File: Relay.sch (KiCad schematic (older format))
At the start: 12 parts

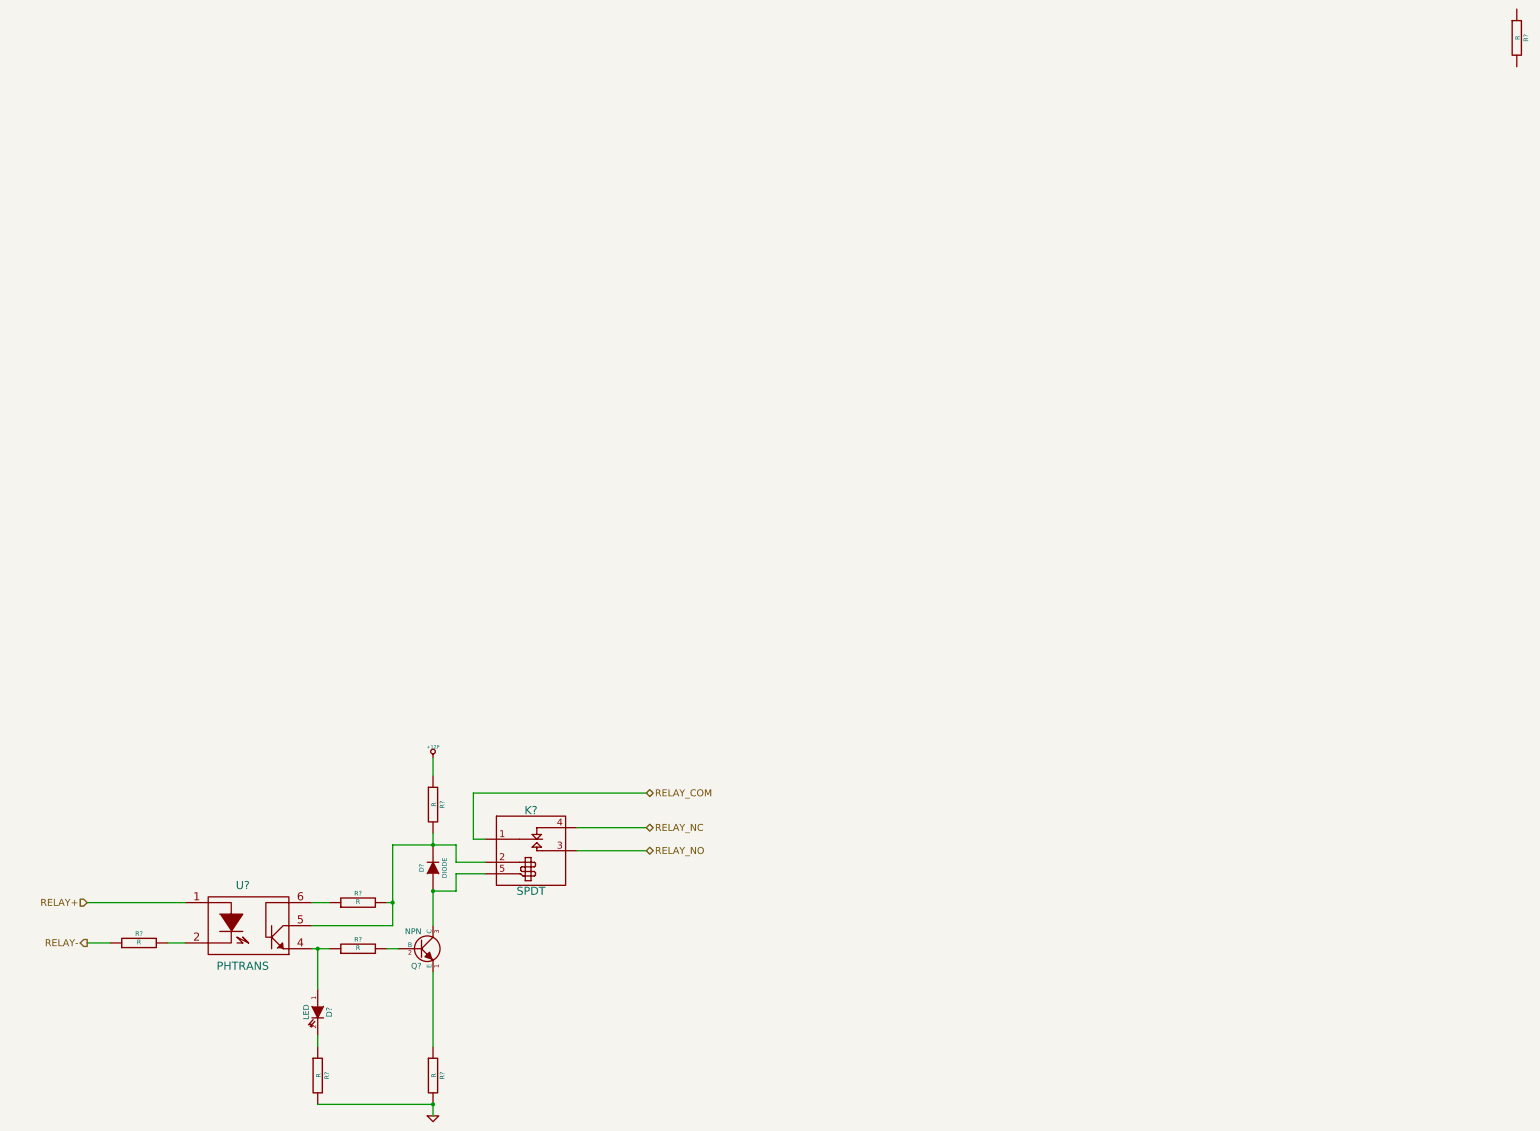
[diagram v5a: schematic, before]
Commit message: Preliminary Module Layouts
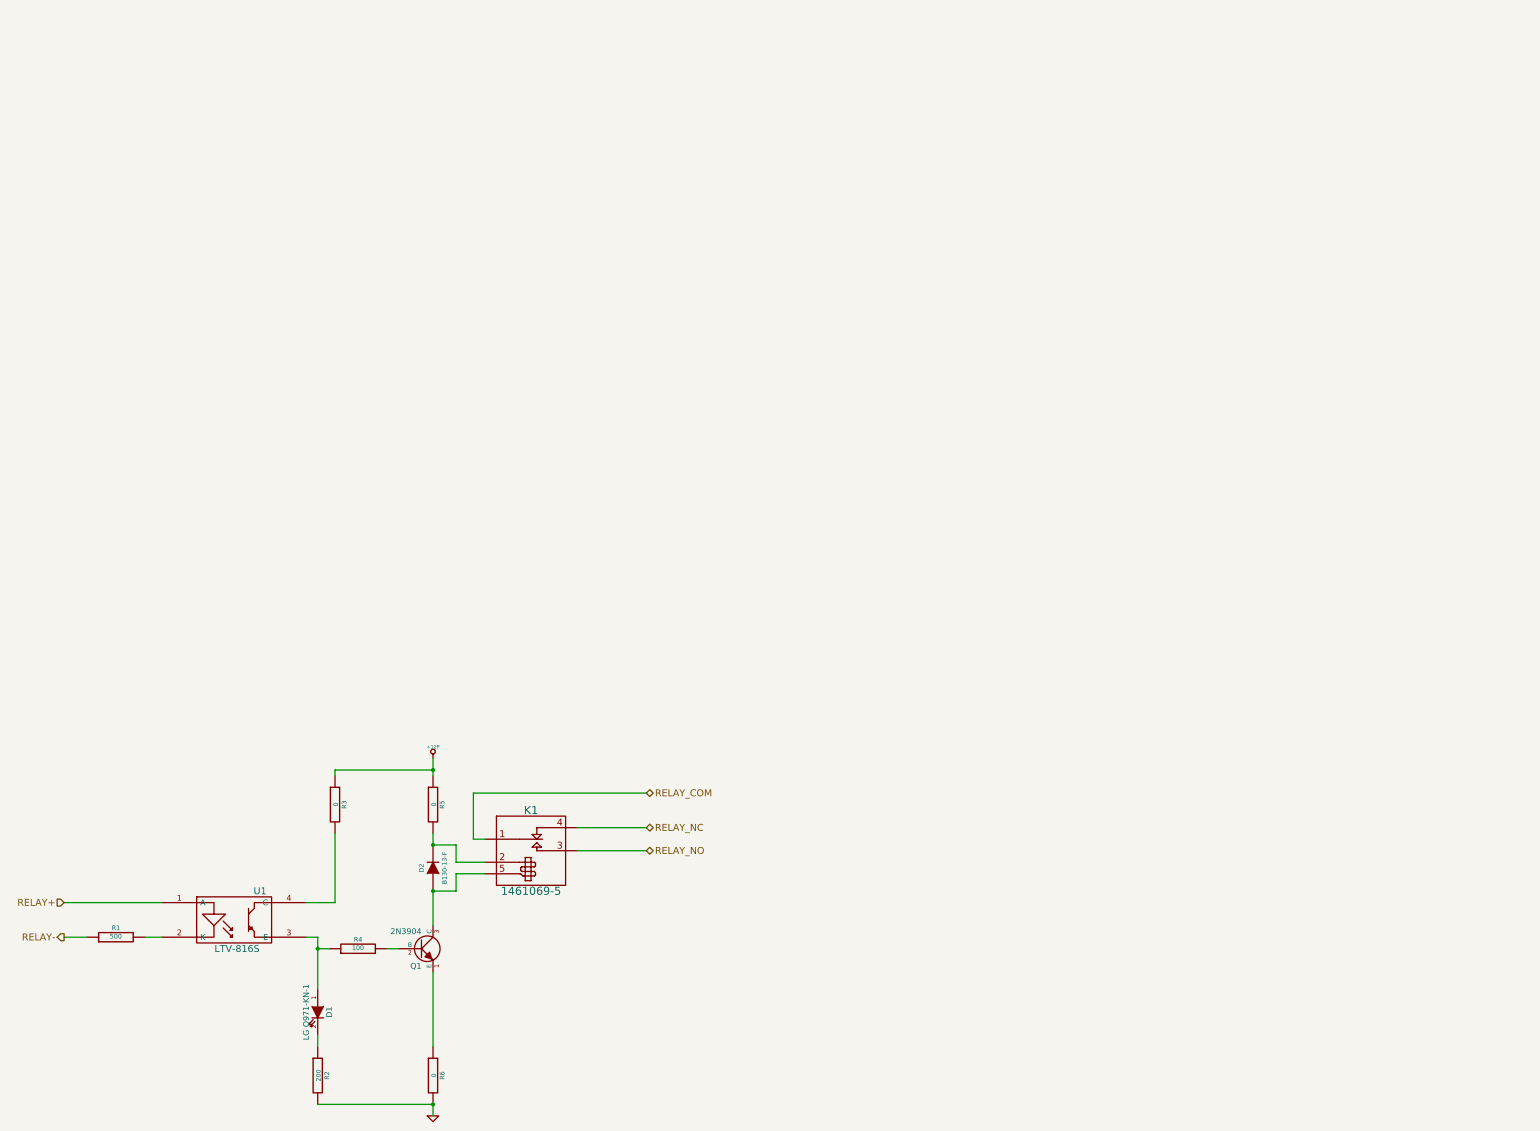
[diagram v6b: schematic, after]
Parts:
- removed R? (x2): R, ~, symbol R
- removed U?: PHTRANS, ~, symbol PHTRANS
- added R3: 0, ~, symbol R
- added U1: LTV-816S, symbol OPTO-TRANSISTOR4
- D1: renamed from D?; value LED -> LG Q971-KN-1
- D2: renamed from D?; value DIODE -> B130-13-F
- K1: renamed from K?; value SPDT -> 1461069-5; MFG Part Number (none) -> 1461069-5
- Q1: renamed from Q?; value NPN -> 2N3904; MFG Name (none) -> Diodes Inc; MFG Part Number (none) -> MMBT3904-7-F
- R1: renamed from R?; value R -> 500
- R2: renamed from R?; value R -> 200
- R4: renamed from R?; value R -> 100
- R5, R6: renamed from R?; value R -> 0
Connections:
- net +12P: now also R3.1
- net RELAY+: now also U1.1 (A)
- net at R1.2: now also U1.2 (K)
- net at D1.1 (A), R4.1: now also U1.3 (E)
- new net: R3.2, U1.4 (C)
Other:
- moved on the sheet: R1
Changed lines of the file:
@@
 $Descr A4 11693 8268
 encoding utf-8
-Sheet 7 9
+Sheet 6 9
 Title ""
-Date "30 sep 2013"
+Date "15 oct 2013"
 Rev ""
 Comp ""
@@
 Comment4 ""
 $EndDescr
-Text HLabel 4750 3350 0    60   Input ~ 0
+Text HLabel 4550 3350 0    60   Input ~ 0
 RELAY+
-Text HLabel 4750 3700 0    60   Output ~ 0
+Text HLabel 4550 3650 0    60   Output ~ 0
 RELAY-
 Text HLabel 9600 2700 2    60   BiDi ~ 0
@@
 Text HLabel 9600 2900 2    60   BiDi ~ 0
 RELAY_NO
-$Comp
-L R R?
-U 1 1 523D0C55
-P 17150 -4150
-F 0 "R?" V 17230 -4150 40  0000 C CNN
-F 1 "R" V 17157 -4149 40  0000 C CNN
-F 2 "~" V 17080 -4150 30  0000 C CNN
-F 3 "~" H 17150 -4150 30  0000 C CNN
-	1    17150 -4150
-	1    0    0    -1
-$EndComp
 Text HLabel 9600 2400 2    60   BiDi ~ 0
 RELAY_COM
 $Comp
-L SPDT K?
+L SPDT K1
 U 1 1 523D17C5
 P 8600 2750
-F 0 "K?" H 8600 2950 70  0000 C CNN
-F 1 "SPDT" H 8600 2250 70  0000 C CNN
+F 0 "K1" H 8600 2950 70  0000 C CNN
+F 1 "1461069-5	" H 8600 2250 70  0000 C CNN
 F 2 "~" H 8600 2750 60  0000 C CNN
 F 3 "~" H 8600 2750 60  0000 C CNN
+F 4 "1461069-5" H 8600 2750 60  0001 C CNN "MFG Part Number"
 	1    8600 2750
 	1    0    0    -1
 $EndComp
 $Comp
-L NPN Q?
+L NPN Q1
 U 1 1 523D17DC
 P 7650 3750
-F 0 "Q?" H 7650 3600 50  0000 R CNN
-F 1 "NPN" H 7650 3900 50  0000 R CNN
+F 0 "Q1" H 7650 3600 50  0000 R CNN
+F 1 "2N3904" H 7650 3900 50  0000 R CNN
 F 2 "~" H 7650 3750 60  0000 C CNN
 F 3 "~" H 7650 3750 60  0000 C CNN
+F 4 "Diodes Inc" H 7650 3750 60  0001 C CNN "MFG Name"
+F 5 "MMBT3904-7-F" H 7650 3750 60  0001 C CNN "MFG Part Number"
 	1    7650 3750
 	1    0    0    -1
 $EndComp
 $Comp
-L DIODE D?
+L DIODE D2
 U 1 1 523D17F8
 P 7750 3050
-F 0 "D?" H 7750 3150 40  0000 C CNN
-F 1 "DIODE" H 7750 2950 40  0000 C CNN
+F 0 "D2" H 7750 3150 40  0000 C CNN
+F 1 "B130-13-F" H 7750 2950 40  0000 C CNN
 F 2 "~" H 7750 3050 60  0000 C CNN
 F 3 "~" H 7750 3050 60  0000 C CNN
@@
 $EndComp
 $Comp
-L R R?
+L R R2
 U 1 1 523D1807
 P 6750 4850
-F 0 "R?" V 6830 4850 40  0000 C CNN
-F 1 "R" V 6757 4851 40  0000 C CNN
+F 0 "R2" V 6830 4850 40  0000 C CNN
+F 1 "200" V 6757 4851 40  0000 C CNN
 F 2 "~" V 6680 4850 30  0000 C CNN
 F 3 "~" H 6750 4850 30  0000 C CNN
@@
 $EndComp
 $Comp
-L PHTRANS U?
-U 1 1 523D1825
-P 6150 3550
-F 0 "U?" H 6100 3900 70  0000 C CNN
-F 1 "PHTRANS" H 6100 3200 70  0000 C CNN
-F 2 "~" H 6150 3550 60  0000 C CNN
-F 3 "~" H 6150 3550 60  0000 C CNN
-	1    6150 3550
-	1    0    0    -1
-$EndComp
-$Comp
-L LED D?
+L LED D1
 U 1 1 523D1884
 P 6750 4300
-F 0 "D?" H 6750 4400 50  0000 C CNN
-F 1 "LED" H 6750 4200 50  0000 C CNN
+F 0 "D1" H 6750 4400 50  0000 C CNN
+F 1 "LG Q971-KN-1" H 6750 4200 50  0000 C CNN
 F 2 "~" H 6750 4300 60  0000 C CNN
 F 3 "~" H 6750 4300 60  0000 C CNN
@@
 $EndComp
 $Comp
-L R R?
+L R R6
 U 1 1 523D18B1
 P 7750 4850
-F 0 "R?" V 7830 4850 40  0000 C CNN
-F 1 "R" V 7757 4851 40  0000 C CNN
+F 0 "R6" V 7830 4850 40  0000 C CNN
+F 1 "0" V 7757 4851 40  0000 C CNN
 F 2 "~" V 7680 4850 30  0000 C CNN
 F 3 "~" H 7750 4850 30  0000 C CNN
@@
 $EndComp
 $Comp
-L GND #PWR?
+L GND #PWR041
 U 1 1 523D18C2
 P 7750 5200
-F 0 "#PWR?" H 7750 5200 30  0001 C CNN
+F 0 "#PWR041" H 7750 5200 30  0001 C CNN
 F 1 "GND" H 7750 5130 30  0001 C CNN
 F 2 "" H 7750 5200 60  0000 C CNN
@@
 	9000 2900 9600 2900
 Wire Wire Line
-	7400 2850 7950 2850
-Wire Wire Line
 	7950 2850 7950 3000
 Wire Wire Line
@@
 	7950 3100 7950 3250
 $Comp
-L R R?
+L R R4
 U 1 1 523D1A7F
 P 7100 3750
-F 0 "R?" V 7180 3750 40  0000 C CNN
-F 1 "R" V 7107 3751 40  0000 C CNN
+F 0 "R4" V 7180 3750 40  0000 C CNN
+F 1 "100" V 7107 3751 40  0000 C CNN
 F 2 "~" V 7030 3750 30  0000 C CNN
 F 3 "~" H 7100 3750 30  0000 C CNN
@@
 $EndComp
 Wire Wire Line
-	6700 3750 6850 3750
-Wire Wire Line
 	7350 3750 7450 3750
 Wire Wire Line
@@
 	6750 4600 6750 4500
 Wire Wire Line
-	6750 4100 6750 3750
+	6750 3650 6750 4100
 Connection ~ 6750 3750
 Wire Wire Line
 	7750 3950 7750 4600
 $Comp
-L R R?
+L R R5
 U 1 1 523D1BDA
 P 7750 2500
-F 0 "R?" V 7830 2500 40  0000 C CNN
-F 1 "R" V 7757 2501 40  0000 C CNN
+F 0 "R5" V 7830 2500 40  0000 C CNN
+F 1 "0" V 7757 2501 40  0000 C CNN
 F 2 "~" V 7680 2500 30  0000 C CNN
 F 3 "~" H 7750 2500 30  0000 C CNN
@@
 Wire Wire Line
 	7950 3250 7750 3250
-Wire Wire Line
-	6700 3550 7400 3550
-Wire Wire Line
-	7400 3550 7400 2850
 Connection ~ 7750 2850
 $Comp
-L R R?
-U 1 1 523D1CFB
-P 7100 3350
-F 0 "R?" V 7180 3350 40  0000 C CNN
-F 1 "R" V 7107 3351 40  0000 C CNN
-F 2 "~" V 7030 3350 30  0000 C CNN
-F 3 "~" H 7100 3350 30  0000 C CNN
-	1    7100 3350
+L R R1
+U 1 1 523D1D41
+P 5000 3650
+F 0 "R1" V 5080 3650 40  0000 C CNN
+F 1 "500" V 5007 3651 40  0000 C CNN
+F 2 "~" V 4930 3650 30  0000 C CNN
+F 3 "~" H 5000 3650 30  0000 C CNN
+	1    5000 3650
 	0    -1   -1   0
 $EndComp
 Wire Wire Line
-	6700 3350 6850 3350
-Wire Wire Line
-	7350 3350 7400 3350
-Connection ~ 7400 3350
-$Comp
-L R R?
-U 1 1 523D1D41
-P 5200 3700
-F 0 "R?" V 5280 3700 40  0000 C CNN
-F 1 "R" V 5207 3701 40  0000 C CNN
-F 2 "~" V 5130 3700 30  0000 C CNN
-F 3 "~" H 5200 3700 30  0000 C CNN
-	1    5200 3700
-	0    -1   -1   0
-$EndComp
-Wire Wire Line
-	5450 3700 5600 3700
-Wire Wire Line
-	4950 3700 4750 3700
-Wire Wire Line
-	4750 3350 5600 3350
-$Comp
-L +12P #PWR?
+	5250 3650 5400 3650
+Wire Wire Line
+	4750 3650 4550 3650
+Wire Wire Line
+	4550 3350 5400 3350
+$Comp
+L +12P #PWR042
 U 1 1 523E67FE
 P 7750 2100
-F 0 "#PWR?" H 7750 2070 30  0001 C CNN
+F 0 "#PWR042" H 7750 2070 30  0001 C CNN
 F 1 "+12P" H 7750 2200 30  0000 C CNN
 F 2 "" H 7750 2100 60  0000 C CNN
@@
 	1    0    0    -1
 $EndComp
+$Comp
+L OPTO-TRANSISTOR4 U1
+U 1 1 525A769C
+P 6050 3500
+F 0 "U1" H 6250 3750 60  0000 C CNN
+F 1 "LTV-816S" H 6050 3250 60  0000 C CNN
+F 2 "" H 6050 3500 60  0000 C CNN
+F 3 "" H 6050 3500 60  0000 C CNN
+	1    6050 3500
+	1    0    0    -1
+$EndComp
+Wire Wire Line
+	6650 3650 6750 3650
+Wire Wire Line
+	6750 3750 6850 3750
+$Comp
+L R R3
+U 1 1 525A7A65
+P 6900 2500
+F 0 "R3" V 6980 2500 40  0000 C CNN
+F 1 "0" V 6907 2501 40  0000 C CNN
+F 2 "~" V 6830 2500 30  0000 C CNN
+F 3 "~" H 6900 2500 30  0000 C CNN
+	1    6900 2500
+	1    0    0    -1
+$EndComp
+Connection ~ 7750 2200
+Wire Wire Line
+	7750 2850 7950 2850
+Wire Wire Line
+	6650 3350 6900 3350
+Wire Wire Line
+	6900 3350 6900 2750
+Wire Wire Line
+	6900 2250 6900 2200
+Wire Wire Line
+	6900 2200 7750 2200
 $EndSCHEMATC
